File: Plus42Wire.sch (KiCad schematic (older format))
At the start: 32 parts, among them CN1 EDGE_CONN, CN2 CONN_I2C_1, CN3 CONN_I2C_1, CN4 CONN_I2C_1, U1 GAL20V8, U2 PCF8584, U3 24LC16, U4 DS1307+, Y1 12 MHz, Y2 32768 kHz

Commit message: Add 3.3V bus
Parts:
- added C10: 10u, Capacitor_THT:CP_Radial_D6.3mm_P2.50mm, symbol Device:CP1
- added C8, C9: 100n, Capacitor_THT:C_Disc_D7.0mm_W2.5mm_P5.00mm, symbol Device:C
- added CN5, CN6, CN7: CONN_I2C_3V3, Connector_PinHeader_2.54mm:PinHeader_1x04_P2.54mm_Vertical, symbol Connector:Conn_01x04_Male
- added Q1, Q2: TN2106, Package_TO_SOT_THT:TO-92L_HandSolder, symbol Device:Q_NMOS_SGD
- added R5, R6: 4.7k, Resistor_THT:R_Axial_DIN0207_L6.3mm_D2.5mm_P10.16mm_Horizontal, symbol Device:R
- added U5: MCP1700-3302E_TO92, Package_TO_SOT_THT:TO-92L_HandSolder, symbol Regulator_Linear:MCP1700-3302E_TO92
- C1, C3, C4, C5, C6, FB1, FB2, JP2, Y1: Notes OPL -> (none)
- C2, C7, CN1, U1: Notes COMMON -> (none)
- CN2, CN3, CN4: value CONN_I2C_1 -> CONN_I2C_5V
- JP3, JP4, JP5, JP6: MouserPN (none) -> -
- R4: renamed from R7; footprint Resistor_THT:R_Axial_DIN0207_L6.3mm_D2.5mm_P2.54mm_Vertical -> Resistor_THT:R_Axial_DIN0207_L6.3mm_D2.5mm_P10.16mm_Horizontal; Notes OPL -> (none)
- V0, V1: Notes - -> (none)
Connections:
- net +5V: now also C8.1, U5.2 (VI)
- net GND: now also C10.2, C8.2, C9.2, CN5.1 (Pin_1), CN6.1 (Pin_1), CN7.1 (Pin_1), U5.1 (GND)
- net scl: now also Q1.3 (D)
- net sda: now also Q2.3 (D)
- net at U4.1 (X1): now also Y2.1; no longer Y2.2
- net at U4.2 (X2): now also Y2.2; no longer Y2.1
- new net +3V3: C10.1, C9.1, CN5.2 (Pin_2), CN6.2 (Pin_2), CN7.2 (Pin_2), Q1.2 (G), Q2.2 (G), R5.1, R6.1, U5.3 (VO)
- new net scl_3v3: CN5.4 (Pin_4), CN6.4 (Pin_4), CN7.4 (Pin_4), Q1.1 (S), R5.2
- new net sda_3v3: CN5.3 (Pin_3), CN6.3 (Pin_3), CN7.3 (Pin_3), Q2.1 (S), R6.2
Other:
- note added: "3.3V BUS LEVEL SHIFTER"
- note added: "3.3V GENERATION"
- note added: "If you want to use a different\nregulator, check the pinout!!!\nMCP1700 is cool since it can\nprovide up to 250 mA, but it\nuses a different pinout than\nmost alternatives!"
- note added: "Key parameters for these MOSFETs:\n- Type: N-channel enhancement mode\n- Gate threshold voltage (VGS(th)): min. 0.1V, max. 2V\n- On resistance (RDS(on)): max. 100 Ohm @ ID= 3mA, VGS= 2.5V\n- Input capacitance (Ciss): max. 100 pF\n- Switching times (ton/toff): max. 50 ns.\n- Allowed drain current (ID): 10 mA or higher\n\nSee Philips/NXP AN97055 for more information.\n\nExamples: TN2106, TN5325, BS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"
- moved on the sheet: BAT1, C3, C4, C5, C6, FB1, FB2, JP1, JP2, JP3, JP4, JP5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

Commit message: Ready for V1rc1
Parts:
- C10: footprint Capacitor_THT:CP_Radial_D6.3mm_P2.50mm -> Capacitor_THT:CP_Radial_D5.0mm_P2.00mm
- CN4: value CONN_I2C_5V -> CONN_I2C_5V_ALT
- CN7: value CONN_I2C_3V3 -> CONN_I2C_3V3_ALT
- V1: footprint (none) -> Plus42Wire:Logo
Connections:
- net +3V3: now also CN7.1 (Pin_1); no longer CN7.2 (Pin_2)
- net +5V: now also CN4.1 (Pin_1); no longer CN4.2 (Pin_2)
- net GND: now also CN4.2 (Pin_2), CN7.2 (Pin_2); no longer CN4.1 (Pin_1), CN7.1 (Pin_1)
- net scl: now also CN4.3 (Pin_3); no longer CN4.4 (Pin_4)
- net scl_3v3: now also CN7.3 (Pin_3); no longer CN7.4 (Pin_4)
- net sda: now also CN4.4 (Pin_4); no longer CN4.3 (Pin_3)
- net sda_3v3: now also CN7.4 (Pin_4); no longer CN7.3 (Pin_3)
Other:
- note added: "*** WARNING! ***\nDIFFERENT\nPINOUT!"
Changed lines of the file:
@@
 F 0 "V1" H 15288 9751 50  0000 L CNN
 F 1 "LOGO" H 15288 9660 50  0000 L CNN
-F 2 "" H 15210 9705 50  0001 C CNN
+F 2 "Plus42Wire:Logo" H 15210 9705 50  0001 C CNN
 F 3 "" H 15210 9705 50  0001 C CNN
 F 4 "-" H 15210 9705 50  0001 C CNN "MouserPN"
@@
 P 13840 4490
 F 0 "CN4" H 13812 4372 50  0000 R CNN
-F 1 "CONN_I2C_5V" H 13812 4463 50  0000 R CNN
+F 1 "CONN_I2C_5V_ALT" H 13812 4463 50  0000 R CNN
 F 2 "Connector_PinHeader_2.54mm:PinHeader_1x04_P2.54mm_Vertical" H 13840 4490 50  0001 C CNN
 F 3 "~" H 13840 4490 50  0001 C CNN
@@
 	1    0    0    1
 $EndComp
+Text Label 14365 4290 2    50   ~ 0
+sda
 Text Label 14365 4390 2    50   ~ 0
-sda
-Text Label 14365 4290 2    50   ~ 0
 scl
 Wire Wire Line
@@
 Wire Wire Line
 	14040 4590 14125 4590
-Wire Wire Line
-	14125 4590 14125 4690
 $Comp
 L power:GND #PWR022
 U 1 1 66FF8A88
-P 14125 4690
-F 0 "#PWR022" H 14125 4440 50  0001 C CNN
-F 1 "GND" H 14130 4517 50  0000 C CNN
-F 2 "" H 14125 4690 50  0001 C CNN
-F 3 "" H 14125 4690 50  0001 C CNN
-	1    14125 4690
+P 14225 4690
+F 0 "#PWR022" H 14225 4440 50  0001 C CNN
+F 1 "GND" H 14230 4517 50  0000 C CNN
+F 2 "" H 14225 4690 50  0001 C CNN
+F 3 "" H 14225 4690 50  0001 C CNN
+	1    14225 4690
 	-1   0    0    -1
 $EndComp
-Wire Wire Line
-	14040 4490 14125 4490
-Wire Wire Line
-	14125 4490 14125 4170
 $Comp
 L power:+5V #PWR021
@@
 F 0 "C10" H 4515 9366 50  0000 L CNN
 F 1 "10u" H 4515 9275 50  0000 L CNN
-F 2 "Capacitor_THT:CP_Radial_D6.3mm_P2.50mm" H 4400 9320 50  0001 C CNN
+F 2 "Capacitor_THT:CP_Radial_D5.0mm_P2.00mm" H 4400 9320 50  0001 C CNN
 F 3 "~" H 4400 9320 50  0001 C CNN
 F 4 "710-860020573008" H 4400 9320 50  0001 C CNN "MouserPN"
@@
 P 13840 8005
 F 0 "CN7" H 13812 7887 50  0000 R CNN
-F 1 "CONN_I2C_3V3" H 13812 7978 50  0000 R CNN
+F 1 "CONN_I2C_3V3_ALT" H 13812 7978 50  0000 R CNN
 F 2 "Connector_PinHeader_2.54mm:PinHeader_1x04_P2.54mm_Vertical" H 13840 8005 50  0001 C CNN
 F 3 "~" H 13840 8005 50  0001 C CNN
@@
 Wire Wire Line
 	14040 8105 14125 8105
-Wire Wire Line
-	14125 8105 14125 8205
 $Comp
 L power:GND #PWR034
 U 1 1 6753BFC8
-P 14125 8205
-F 0 "#PWR034" H 14125 7955 50  0001 C CNN
-F 1 "GND" H 14130 8032 50  0000 C CNN
-F 2 "" H 14125 8205 50  0001 C CNN
-F 3 "" H 14125 8205 50  0001 C CNN
-	1    14125 8205
+P 14225 8205
+F 0 "#PWR034" H 14225 7955 50  0001 C CNN
+F 1 "GND" H 14230 8032 50  0000 C CNN
+F 2 "" H 14225 8205 50  0001 C CNN
+F 3 "" H 14225 8205 50  0001 C CNN
+	1    14225 8205
 	-1   0    0    -1
 $EndComp
-Wire Wire Line
-	14040 8005 14125 8005
-Wire Wire Line
-	14125 8005 14125 7685
 Wire Wire Line
 	14040 5570 14490 5570
@@
 Text Label 14490 6780 2    50   ~ 0
 sda_3v3
+Text Label 14490 7905 2    50   ~ 0
+scl_3v3
 Text Label 14490 7805 2    50   ~ 0
-scl_3v3
-Text Label 14490 7905 2    50   ~ 0
 sda_3v3
 $Comp
@@
 	1    0    0    1
 $EndComp
+Text Notes 2740 10440 0    50   ~ 0
+If you want to use a different\nregulator, check the pinout!!!\nMCP1700 is cool since it can\nprovide up to 250 mA, but it\nuses a different pinout than\nmost alternatives!
+Wire Wire Line
+	14225 4490 14225 4690
+Wire Wire Line
+	14040 4490 14225 4490
+Wire Wire Line
+	14125 4170 14125 4590
+Text Notes 14585 4510 0    50   ~ 0
+*** WARNING! ***\nDIFFERENT\nPINOUT!
+Text Notes 14630 8055 0    50   ~ 0
+*** WARNING! ***\nDIFFERENT\nPINOUT!
+Wire Wire Line
+	14225 8005 14225 8205
+Wire Wire Line
+	14040 8005 14225 8005
+Wire Wire Line
+	14125 7685 14125 8105
 Wire Bus Line
 	7835 1875 7835 3615
@@
 Wire Bus Line
 	5635 1670 5635 3615
-Text Notes 2740 10440 0    50   ~ 0
-If you want to use a different\nregulator, check the pinout!!!\nMCP1700 is cool since it can\nprovide up to 250 mA, but it\nuses a different pinout than\nmost alternatives!
 $EndSCHEMATC

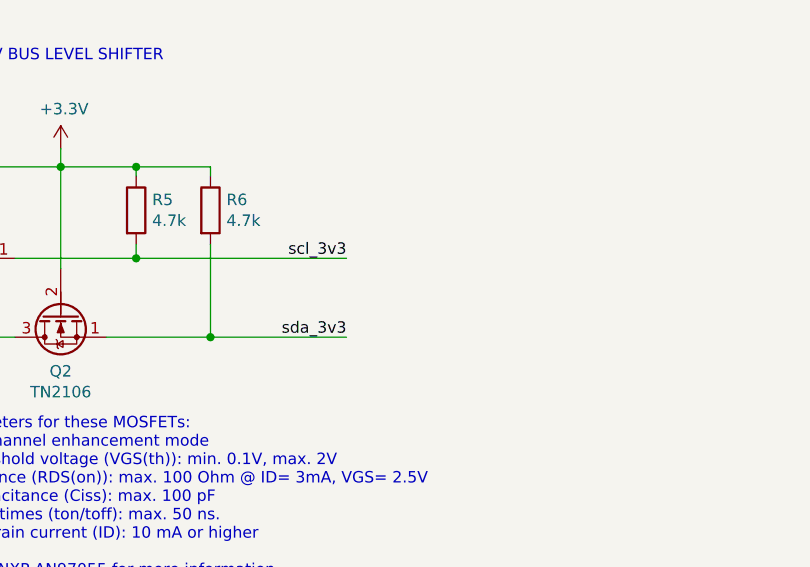
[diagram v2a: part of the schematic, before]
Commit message: Add footprints for alternative MOSFETs
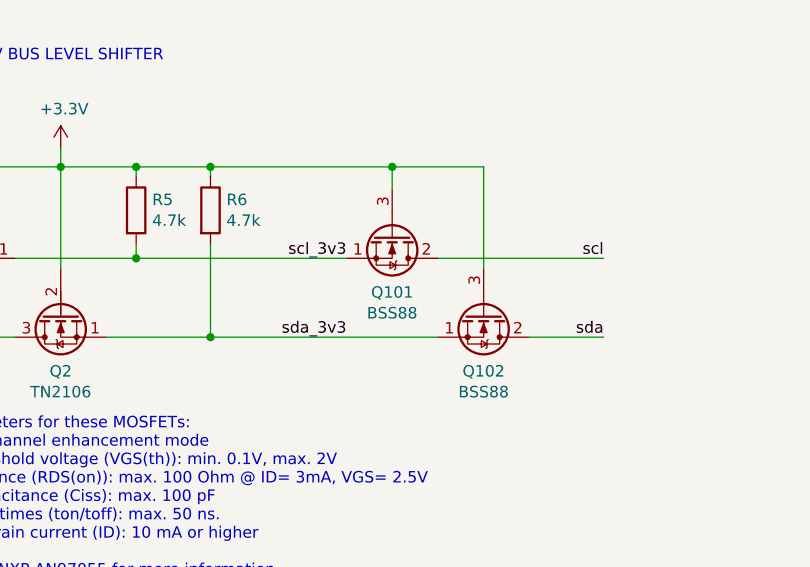
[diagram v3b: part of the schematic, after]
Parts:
- added Q101, Q102: BSS88, Package_TO_SOT_THT:TO-92L_HandSolder, symbol Device:Q_NMOS_SDG
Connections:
- net +3V3: now also Q101.3 (G), Q102.3 (G)
- net scl: now also Q101.2 (D)
- net scl_3v3: now also Q101.1 (S)
- net sda: now also Q102.2 (D)
- net sda_3v3: now also Q102.1 (S)
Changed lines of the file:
@@
 	7370 9475 7825 9475
 Connection ~ 7825 9475
-Wire Wire Line
-	7825 9475 8420 9475
 $Comp
 L Device:R R5
@@
 Wire Wire Line
 	7825 9070 7825 9475
-Wire Wire Line
-	7500 8730 7825 8730
 Wire Wire Line
 	7825 8770 7825 8730
@@
 Wire Wire Line
 	14125 7685 14125 8105
+Wire Wire Line
+	8620 8730 8620 8830
+Text Label 9545 9130 2    50   ~ 0
+scl
+Wire Wire Line
+	9220 9475 9545 9475
+Wire Wire Line
+	7500 8730 7825 8730
+Connection ~ 7825 8730
+$Comp
+L Device:Q_NMOS_SDG Q101
+U 1 1 670206AA
+P 8620 9030
+F 0 "Q101" V 8869 9030 50  0000 C CNN
+F 1 "BSS88" V 8960 9030 50  0000 C CNN
+F 2 "Package_TO_SOT_THT:TO-92L_HandSolder" H 8820 9130 50  0001 C CNN
+F 3 "~" H 8620 9030 50  0001 C CNN
+	1    8620 9030
+	0    1    1    0
+$EndComp
+$Comp
+L Device:Q_NMOS_SDG Q102
+U 1 1 6709143B
+P 9020 9375
+F 0 "Q102" V 9269 9375 50  0000 C CNN
+F 1 "BSS88" V 9360 9375 50  0000 C CNN
+F 2 "Package_TO_SOT_THT:TO-92L_HandSolder" H 9220 9475 50  0001 C CNN
+F 3 "~" H 9020 9375 50  0001 C CNN
+	1    9020 9375
+	0    1    1    0
+$EndComp
+Wire Wire Line
+	9020 9175 9020 8730
+Wire Wire Line
+	7825 8730 8620 8730
+Connection ~ 8620 8730
+Text Label 9545 9475 2    50   ~ 0
+sda
+Wire Wire Line
+	9545 9130 8820 9130
+Wire Wire Line
+	7825 9475 8820 9475
+Wire Wire Line
+	8620 8730 9020 8730
 Wire Bus Line
 	7835 1875 7835 3615
